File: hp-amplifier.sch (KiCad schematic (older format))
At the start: 30 parts, among them J8 Conn_01x02, J9 Conn_01x02, U4 SKY66295, U5 SKY66295

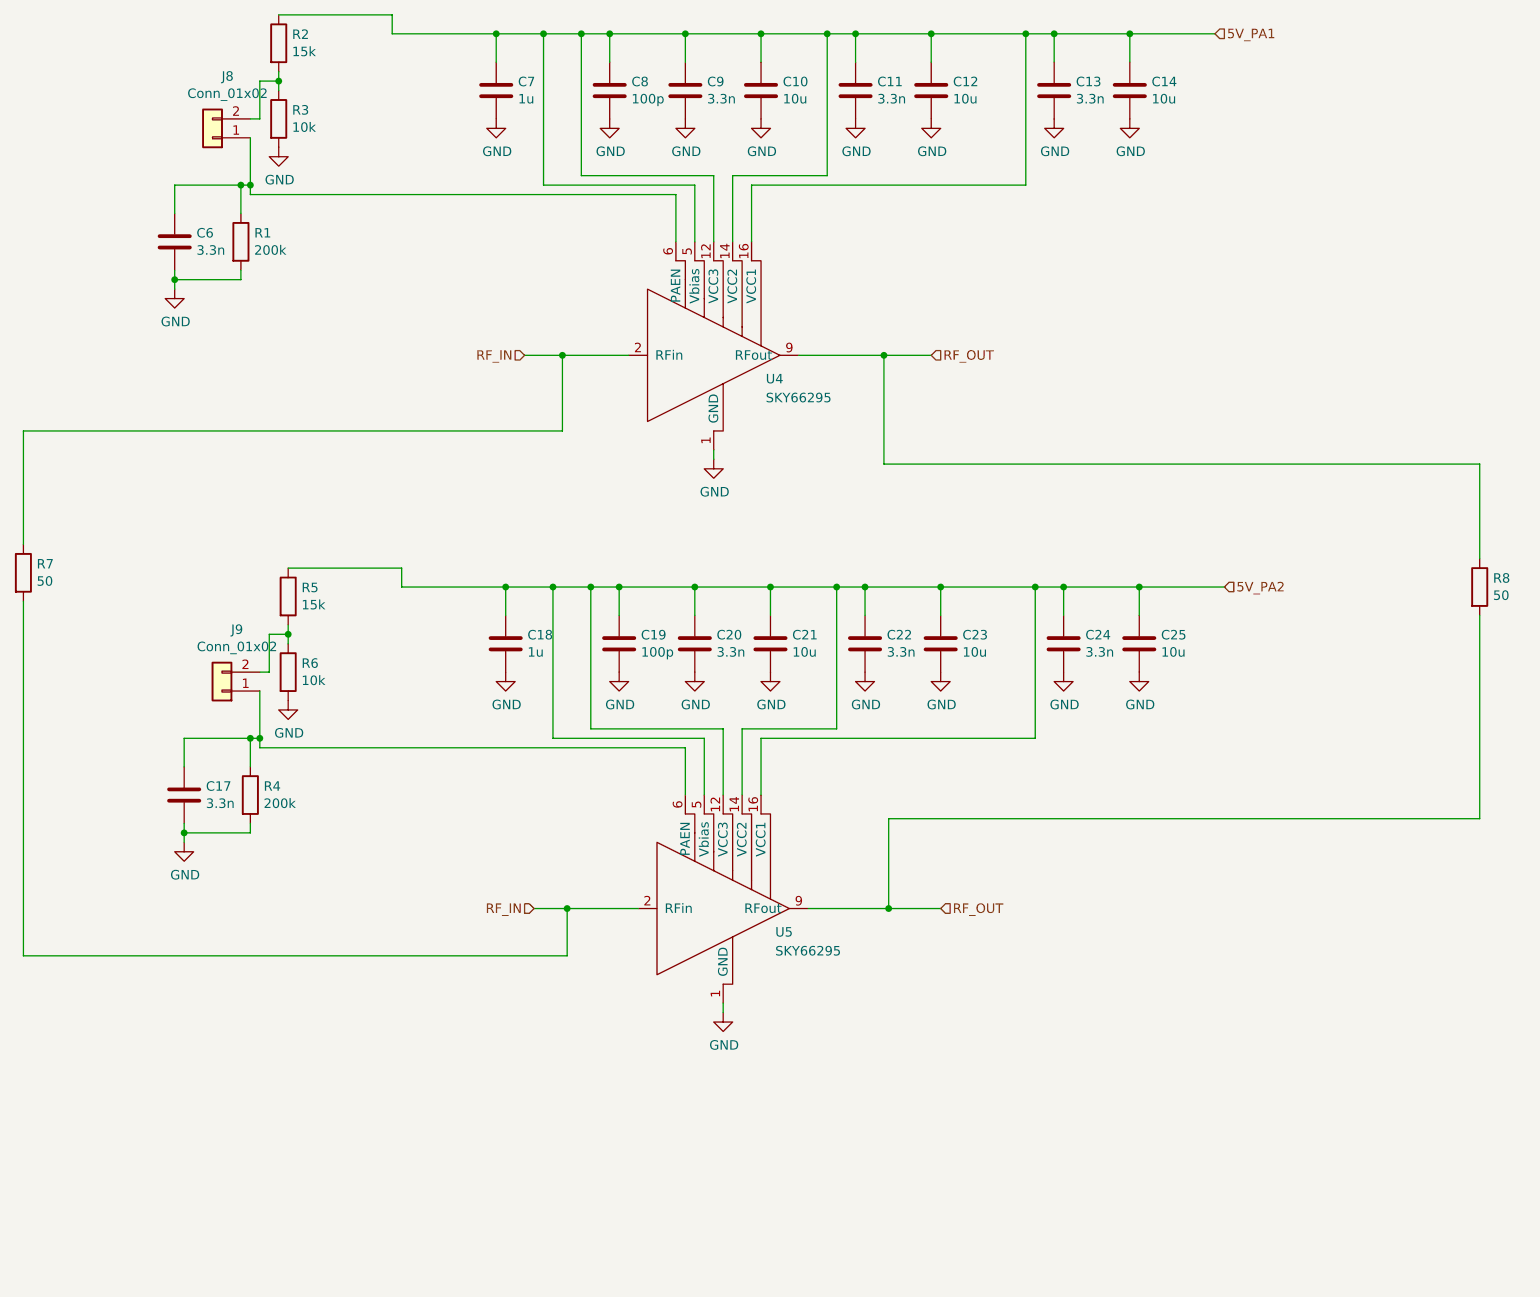
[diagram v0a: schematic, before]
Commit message: done till all routing ground ring and ground plane handeled, only bare copper part is left
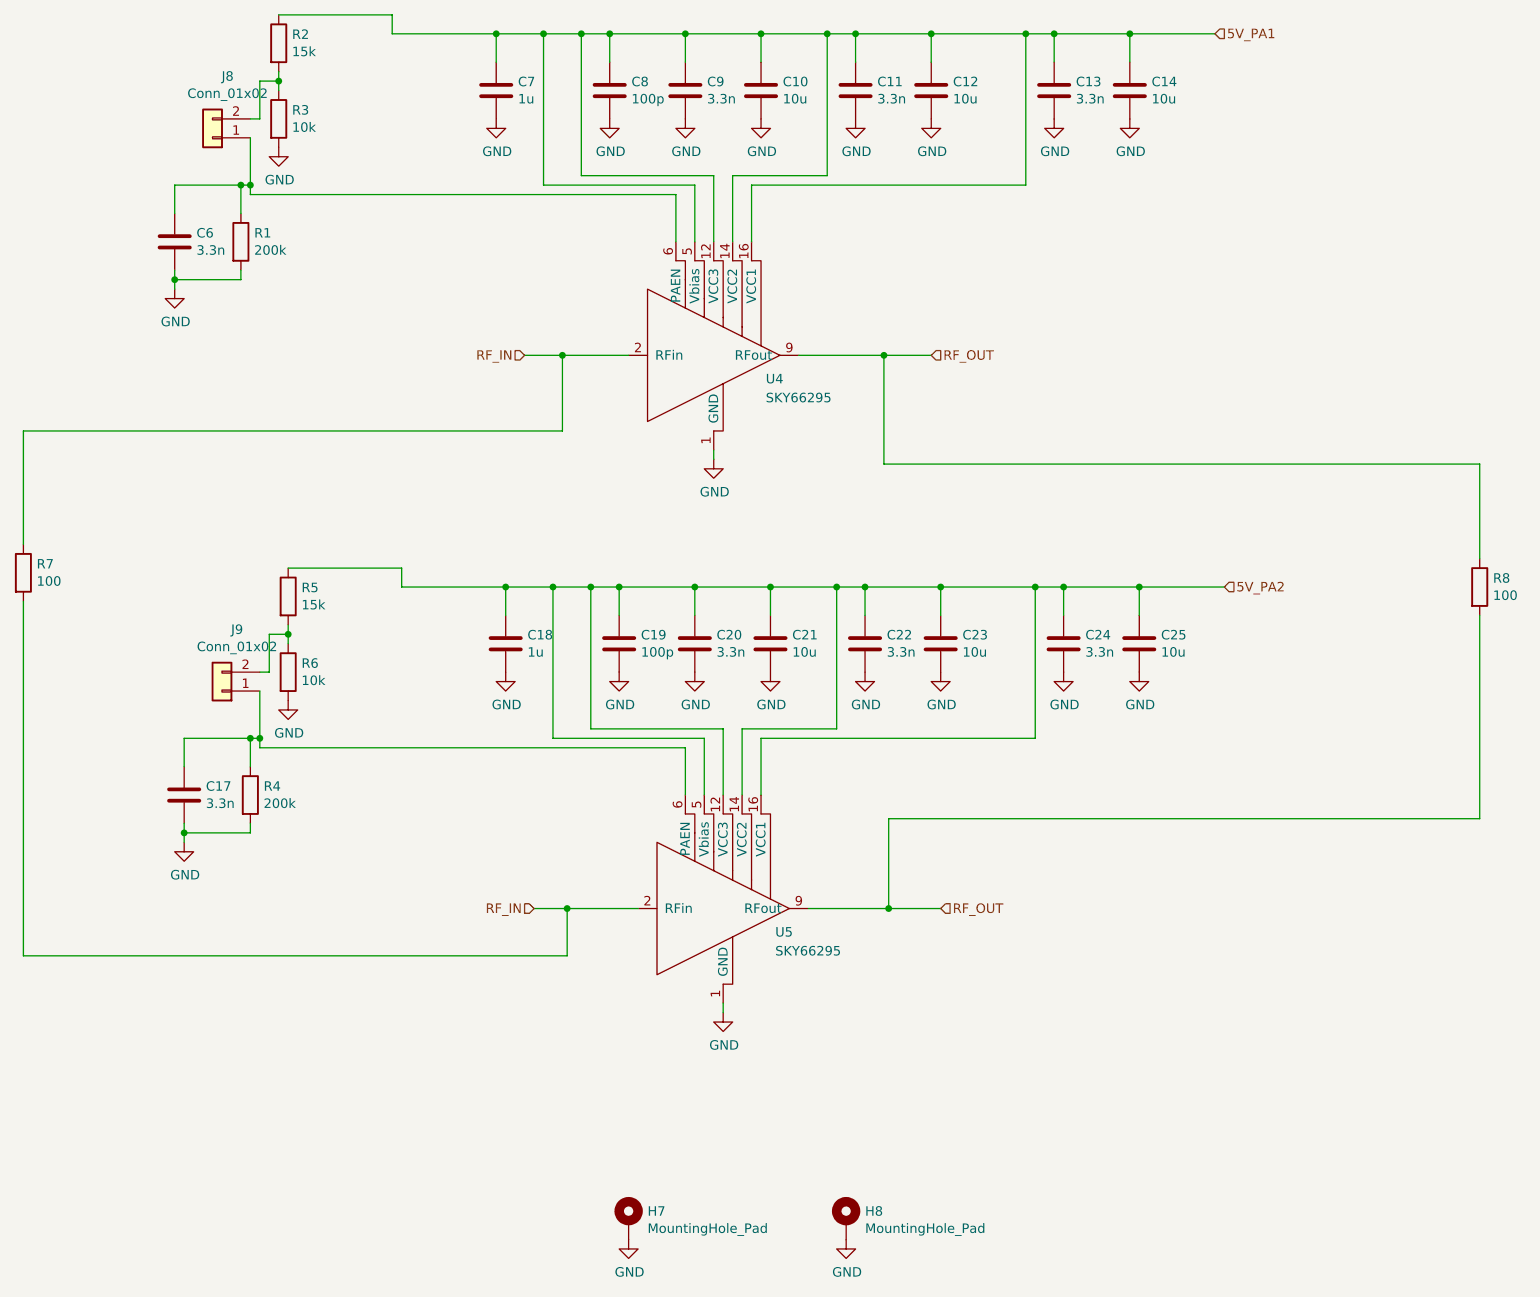
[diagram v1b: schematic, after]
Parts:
- added H7, H8: MountingHole_Pad, MountingHole:MountingHole_3.2mm_M3_Pad_Via, symbol Mechanical:MountingHole_Pad
- J8, J9: footprint Connector_PinHeader_2.54mm:PinHeader_1x02_P2.54mm_Vertical -> Connector_PinHeader_2.54mm:PinHeader_1x02_P2.54mm_Vertical_SMD_Pin1Left
- R7: value 50 -> 100
- R8: value 50 -> 100; footprint Resistor_SMD:R_0603_1608Metric_Pad1.05x0.95mm_HandSolder -> Resistor_SMD:R_2010_5025Metric_Pad1.52x2.65mm_HandSolder
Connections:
- net GND: now also H7.1, H8.1
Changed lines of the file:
@@
 F 0 "J8" H 2220 1350 50  0000 C CNN
 F 1 "Conn_01x02" H 2220 1441 50  0000 C CNN
-F 2 "Connector_PinHeader_2.54mm:PinHeader_1x02_P2.54mm_Vertical" H 2300 1675 50  0001 C CNN
+F 2 "Connector_PinHeader_2.54mm:PinHeader_1x02_P2.54mm_Vertical_SMD_Pin1Left" H 2300 1675 50  0001 C CNN
 F 3 "~" H 2300 1675 50  0001 C CNN
 	1    2300 1675
@@
 F 0 "J9" H 2270 4275 50  0000 C CNN
 F 1 "Conn_01x02" H 2270 4366 50  0000 C CNN
-F 2 "Connector_PinHeader_2.54mm:PinHeader_1x02_P2.54mm_Vertical" H 2350 4600 50  0001 C CNN
+F 2 "Connector_PinHeader_2.54mm:PinHeader_1x02_P2.54mm_Vertical_SMD_Pin1Left" H 2350 4600 50  0001 C CNN
 F 3 "~" H 2350 4600 50  0001 C CNN
 	1    2350 4600
@@
 P 9000 4050
 F 0 "R8" H 9070 4096 50  0000 L CNN
-F 1 "50" H 9070 4005 50  0000 L CNN
-F 2 "Resistor_SMD:R_0603_1608Metric_Pad1.05x0.95mm_HandSolder" V 8930 4050 50  0001 C CNN
+F 1 "100" H 9070 4005 50  0000 L CNN
+F 2 "Resistor_SMD:R_2010_5025Metric_Pad1.52x2.65mm_HandSolder" V 8930 4050 50  0001 C CNN
 F 3 "~" H 9000 4050 50  0001 C CNN
 	1    9000 4050
@@
 P 1300 3975
 F 0 "R7" H 1370 4021 50  0000 L CNN
-F 1 "50" H 1370 3930 50  0000 L CNN
+F 1 "100" H 1370 3930 50  0000 L CNN
 F 2 "Resistor_SMD:R_0603_1608Metric_Pad1.05x0.95mm_HandSolder" V 1230 3975 50  0001 C CNN
 F 3 "~" H 1300 3975 50  0001 C CNN
@@
 Text HLabel 7650 4050 2    50   Input ~ 0
 5V_PA2
+$Comp
+L Mechanical:MountingHole_Pad H?
+U 1 1 5F42D8EC
+P 4500 7400
+AR Path="/5F42D8EC" Ref="H?"  Part="1"
+AR Path="/5F10D9AA/5F42D8EC" Ref="H7"  Part="1"
+F 0 "H7" H 4600 7449 50  0000 L CNN
+F 1 "MountingHole_Pad" H 4600 7358 50  0000 L CNN
+F 2 "MountingHole:MountingHole_3.2mm_M3_Pad_Via" H 4500 7400 50  0001 C CNN
+F 3 "~" H 4500 7400 50  0001 C CNN
+	1    4500 7400
+	1    0    0    -1
+$EndComp
+$Comp
+L Mechanical:MountingHole_Pad H?
+U 1 1 5F42D8F2
+P 5650 7400
+AR Path="/5F42D8F2" Ref="H?"  Part="1"
+AR Path="/5F10D9AA/5F42D8F2" Ref="H8"  Part="1"
+F 0 "H8" H 5750 7449 50  0000 L CNN
+F 1 "MountingHole_Pad" H 5750 7358 50  0000 L CNN
+F 2 "MountingHole:MountingHole_3.2mm_M3_Pad_Via" H 5650 7400 50  0001 C CNN
+F 3 "~" H 5650 7400 50  0001 C CNN
+	1    5650 7400
+	1    0    0    -1
+$EndComp
+$Comp
+L power:GND #PWR?
+U 1 1 5F42D904
+P 4500 7500
+AR Path="/5F42D904" Ref="#PWR?"  Part="1"
+AR Path="/5F10D9AA/5F42D904" Ref="#PWR0114"  Part="1"
+F 0 "#PWR0114" H 4500 7250 50  0001 C CNN
+F 1 "GND" H 4505 7327 50  0000 C CNN
+F 2 "" H 4500 7500 50  0001 C CNN
+F 3 "" H 4500 7500 50  0001 C CNN
+	1    4500 7500
+	1    0    0    -1
+$EndComp
+$Comp
+L power:GND #PWR?
+U 1 1 5F42D90A
+P 5650 7500
+AR Path="/5F42D90A" Ref="#PWR?"  Part="1"
+AR Path="/5F10D9AA/5F42D90A" Ref="#PWR0116"  Part="1"
+F 0 "#PWR0116" H 5650 7250 50  0001 C CNN
+F 1 "GND" H 5655 7327 50  0000 C CNN
+F 2 "" H 5650 7500 50  0001 C CNN
+F 3 "" H 5650 7500 50  0001 C CNN
+	1    5650 7500
+	1    0    0    -1
+$EndComp
 $EndSCHEMATC
